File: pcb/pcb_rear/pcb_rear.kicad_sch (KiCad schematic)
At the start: 23 parts, among them J1 MicroLab Input, J2 Pump, J3 DFRobot O2, J4 DFRobot NH3, Q1 T2N7002AK, Q2 T2N7002AK, Q3 T2N7002AK, Q4 T2N7002AK, U1 USEQGSE CO2, U2 USEQGSE CH4, U3 XC9265A331MR-G, U4 XC9265A331MR-G

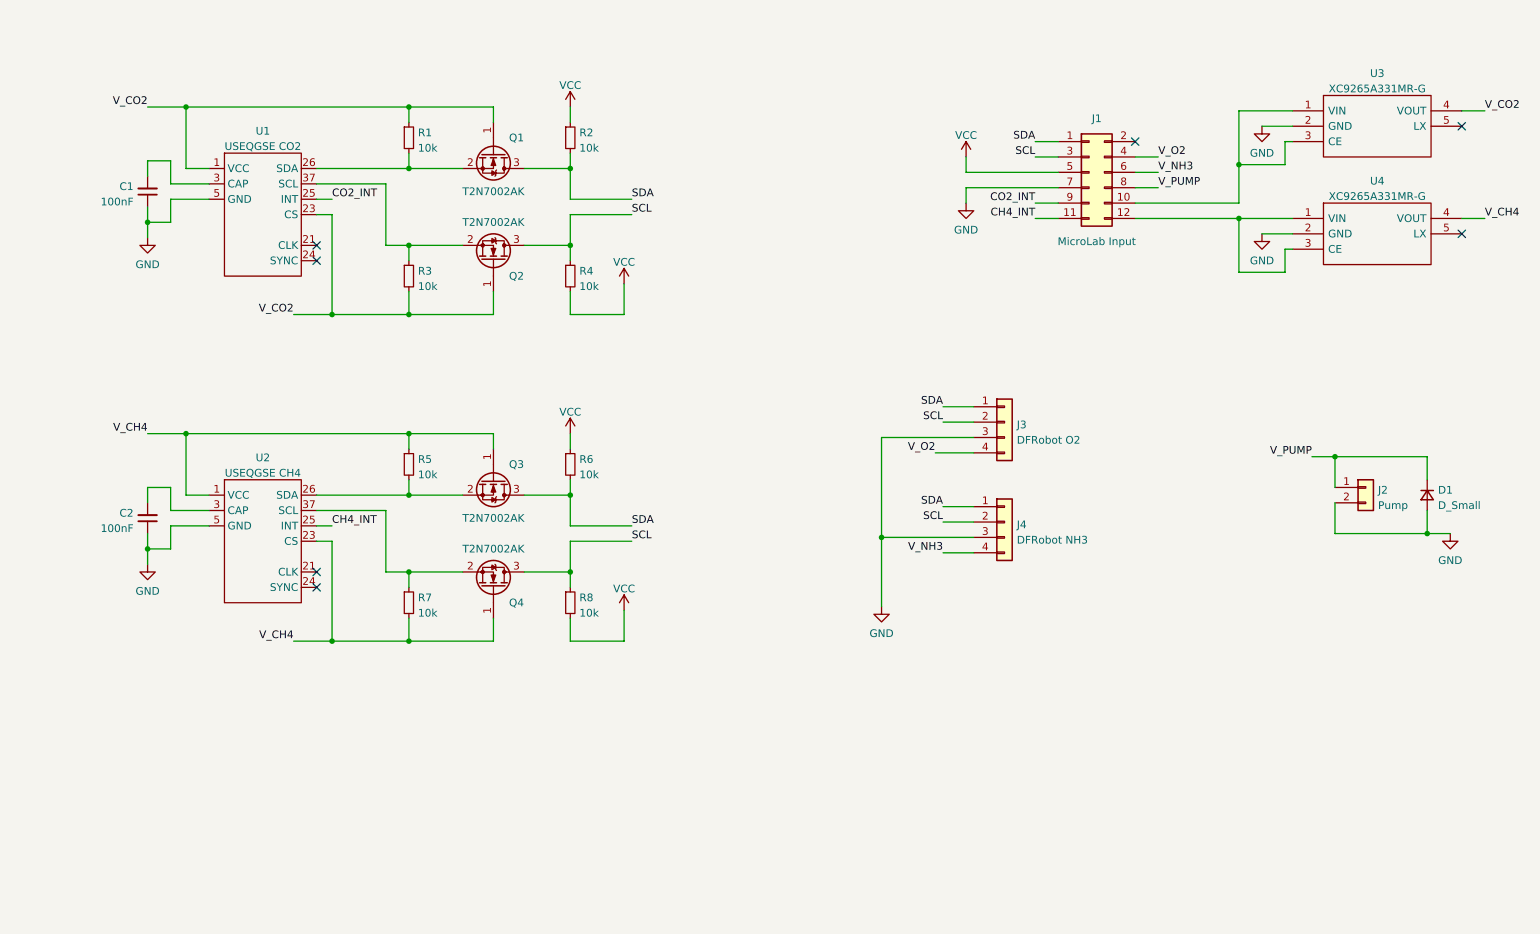
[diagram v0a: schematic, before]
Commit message: renamed pcb
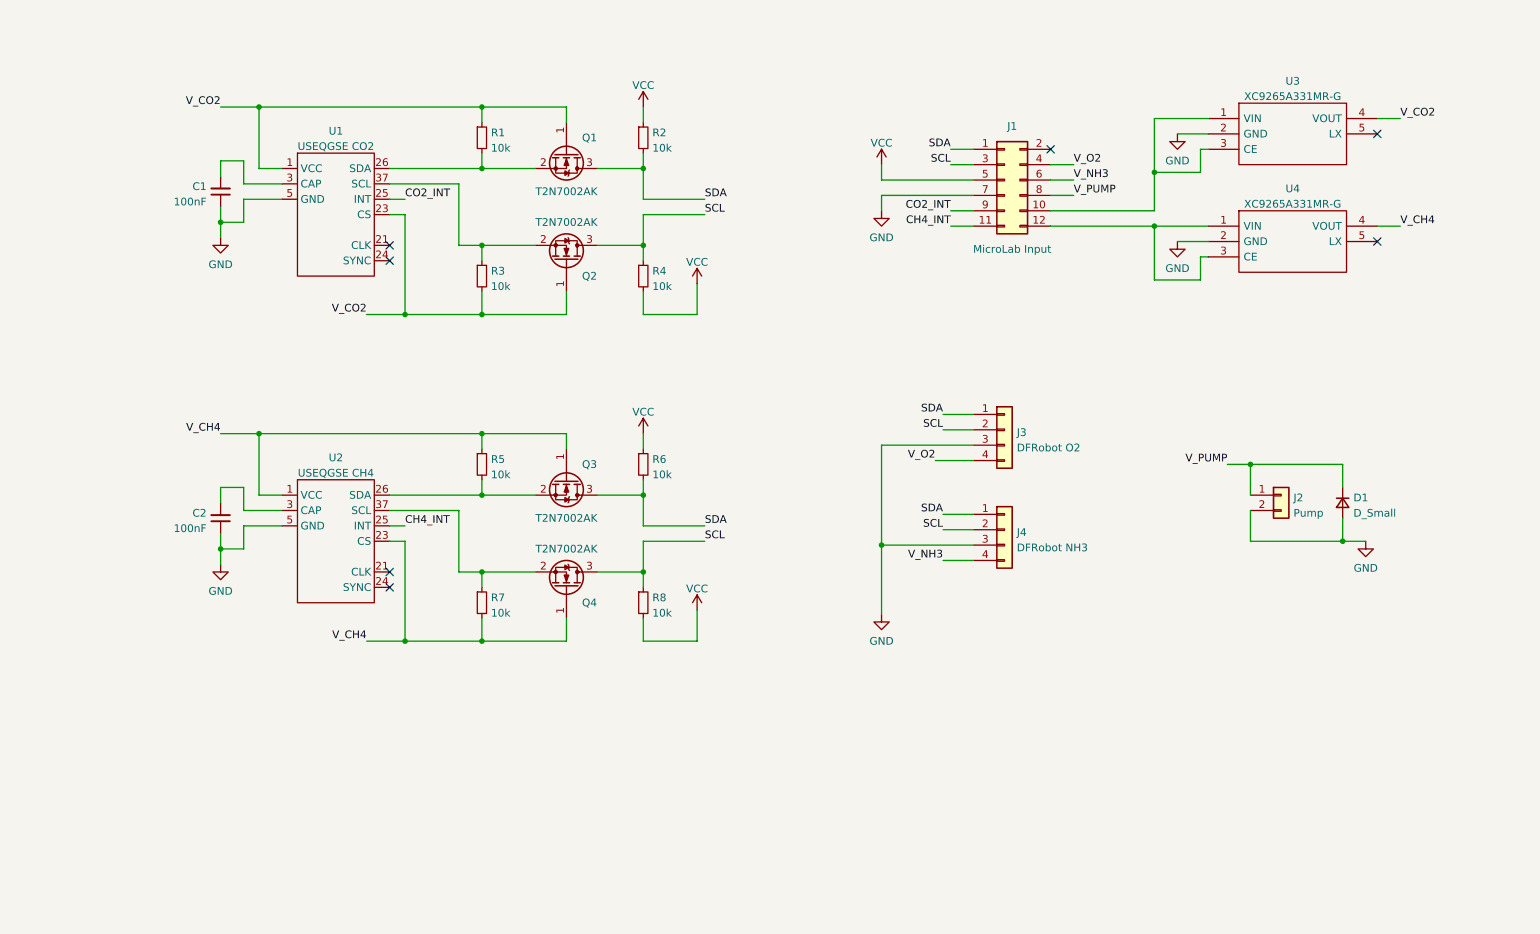
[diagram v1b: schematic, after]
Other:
- moved on the sheet: C1, C2, D1, J1, J2, J3, J4, Q1, Q2, Q3, Q4, R1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

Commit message: front pcb 1st rev
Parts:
- removed U3, U4: XC9265A331MR-G, SamacSys:SOT95P280X130-5N, symbol SamacSys:XC9265A331MR-G
- added D2: D_Small, Diode_SMD:D_0603_1608Metric, symbol Device:D_Small
- added J5: Fan, Connector_PinSocket_2.54mm:PinSocket_1x02_P2.54mm_Vertical, symbol Connector_Generic:Conn_01x02
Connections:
- net GND: now also D2.2 (A), J5.2 (Pin_2)
- net V_CH4: now also J1.12 (Pin_12)
- net V_CO2: now also J1.10 (Pin_10)
- net V_NH3: now also J1.8 (Pin_8); no longer J1.6 (Pin_6)
- net V_O2: now also J1.6 (Pin_6); no longer J1.4 (Pin_4)
- net V_PUMP: now also J1.4 (Pin_4); no longer J1.8 (Pin_8)
- net V_FAN: now reaches J1.2 (Pin_2)
- net V_FAN: now also D2.1 (K), J5.1 (Pin_1)
- no-connect marks 7 -> 4
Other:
- moved on the sheet: D1, J1, J2, J3, J4

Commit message: fin
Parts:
- removed C2: 100nF, Capacitor_SMD:C_0603_1608Metric, symbol Device:C_Small
- removed J1: MicroLab Input, Connector_PinSocket_2.54mm:PinSocket_2x06_P2.54mm_Vertical, symbol Connector_Generic:Conn_02x06_Odd_Even
- removed J2: Pump, Connector_PinSocket_2.54mm:PinSocket_1x02_P2.54mm_Vertical, symbol Connector_Generic:Conn_01x02
- removed J3: DFRobot O2, Connector_PinSocket_2.54mm:PinSocket_1x04_P2.54mm_Vertical, symbol Connector_Generic:Conn_01x04
- removed J4: DFRobot NH3, Connector_PinSocket_2.54mm:PinSocket_1x04_P2.54mm_Vertical, symbol Connector_Generic:Conn_01x04
- removed J5: Fan, Connector_PinSocket_2.54mm:PinSocket_1x02_P2.54mm_Vertical, symbol Connector_Generic:Conn_01x02
- removed Q1, Q2, Q3, Q4: T2N7002AK, Package_TO_SOT_SMD:SOT-23, symbol Transistor_FET:BSS138
- added C1, C3, C5, C6, C7: 0.1uF, Capacitor_SMD:C_0402_1005Metric, symbol Device:C_Small
- added C4, C8: 10uF, Capacitor_SMD:C_0402_1005Metric, symbol Device:C_Small
- added D3: PWR, LED_SMD:LED_0402_1005Metric, symbol Device:LED_Small
- added H1, H2, H3, H4: M2, MountingHole:MountingHole_2.2mm_M2_DIN965_Pad, symbol Mechanical:MountingHole_Pad
- added J1: XIAO_L, Connector_PinSocket_2.54mm:PinSocket_1x07_P2.54mm_Vertical, symbol Connector_Generic:Conn_01x07
- added J2: XIAO_R, Connector_PinSocket_2.54mm:PinSocket_1x07_P2.54mm_Vertical, symbol Connector_Generic:Conn_01x07
- added J3: MicroLab, Connector_JST:JST_SH_BM04B-SRSS-TB_1x04-1MP_P1.00mm_Vertical, symbol Connector_Generic_MountingPin:Conn_01x04_MountingPin
- added J4: O2 Sensor, Connector_JST:JST_SH_BM04B-SRSS-TB_1x04-1MP_P1.00mm_Vertical, symbol Connector_Generic_MountingPin:Conn_01x04_MountingPin
- added J5: Fan, Connector_JST:JST_SH_BM02B-SRSS-TB_1x02-1MP_P1.00mm_Vertical, symbol Connector_Generic_MountingPin:Conn_01x02_MountingPin
- added J8: MEM2051-00-195-00-A, SamacSys:MEM20510019500A, symbol Mouser Parts:MEM2051-00-195-00-A
- added Q1: NX7002BKR, Package_TO_SOT_SMD:SOT-23, symbol Mouser Parts:NX7002BKR
- added R9: 500, Resistor_SMD:R_0402_1005Metric, symbol Device:R_Small
- C2: renamed from C1; value 100nF -> 0.1uF; footprint Capacitor_SMD:C_0603_1608Metric -> Capacitor_SMD:C_0402_1005Metric
- D1, D2: footprint Diode_SMD:D_0603_1608Metric -> Diode_SMD:D_SOD-323
- R1, R2, R3, R4, R5: value 10k -> 50k; footprint Resistor_SMD:R_0603_1608Metric -> Resistor_SMD:R_0402_1005Metric
- R6, R7, R8: footprint Resistor_SMD:R_0603_1608Metric -> Resistor_SMD:R_0402_1005Metric
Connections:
- net V_CH4 is gone; now on net +3.3V: R5.1, R7.2, U2.1 (VCC), U2.23 (CS)
- net GND: now also R8.1, C1.1, C3.1, C4.1, C5.1, C6.1, C7.1, C8.1, D3.1 (K), H1.1, H2.1, H3.1, H4.1, J1.2 (Pin_2), J3.4 (Pin_4), J3.MP (MountPin), J4.2 (Pin_2), J4.MP (MountPin), J8.MP1, J8.MP2, J8.MP3, J8.MP4, J8.MP5, J8.P6 (VSS), Q1.2; no longer D1.2 (A), D2.2 (A)
- net SCL: now also R7.1, U1.27 (SCL), U2.27 (SCL), J2.6 (Pin_6), J4.4 (Pin_4); no longer R4.1, R8.1
- net SDA: now also R6.1, U1.26 (SDA), U2.26 (SDA), J2.5 (Pin_5), J4.3 (Pin_3); no longer R2.2, R6.2
- net at R5.2: now also J8.P8 (DAT1); no longer U2.26 (SDA)
- net +3.3V: now reaches R3.1
- net +3.3V: now also R1.1, R2.1, R4.1, R6.2, U1.1 (VCC), U1.23 (CS), C1.2, C3.2, C4.2, C6.2, C7.2, C8.2, J1.3 (Pin_3), J4.1 (Pin_1), J8.P4 (VDD); no longer U1.37 (SCL)
- net at U2.3 (CAP): now also C5.2
- net at R1.2: now also J8.P1 (DAT2); no longer U1.26 (SDA)
- net CH4_INT: no longer names the net of U2.25 (INT)
- net CO2_INT: no longer names the net of U1.25 (INT)
- removed net VCC: R2.1, R4.2, R6.1, R8.2
- removed net V_CO2: R1.1, R3.2, U1.1 (VCC), U1.23 (CS)
- net V_FAN renamed +5V
- net +5V: now also D1.2 (A), J1.1 (Pin_1), J5.1 (Pin_1), R9.2
- net V_PUMP: no longer names the net of D1.1 (K)
- net V_PUMP: now also J3.1 (Pin_1)
- new net: D2.2 (A), J5.2 (Pin_2), J5.MP (MountPin), Q1.3
- new net: D3.2 (A), R9.1
- new net D0: J2.1 (Pin_1), J8.P2 (CD/DAT3), R2.2
- new net D1: J2.2 (Pin_2), Q1.1, R8.2
- new net MISO: J1.5 (Pin_5), J8.P7 (DAT0), R4.2
- new net MOSI: J1.4 (Pin_4), J8.P3 (CMD), R3.2
- new net P2: J2.3 (Pin_3)
- new net P3: J2.4 (Pin_4)
- new net RX: J2.7 (Pin_7), J3.2 (Pin_2)
- new net SCK: J1.6 (Pin_6), J8.P5 (CLK)
- new net TX: J1.7 (Pin_7), J3.3 (Pin_3)
- no-connect marks 4 -> 6
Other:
- note added: "NOTE: SEEEDUINO XIAO IS 3.3V LOGIC"
- note added: "Protects MicroLab from Seeeduino Xiao USB power"
- moved on the sheet: C2, D2, U1

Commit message: goodnight
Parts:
- R1, R2, R3, R4: value 50k -> 10k
- R9: value 500 -> 2k
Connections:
- net +5V: now also D1.1 (K); no longer D1.2 (A)
- net at J3.1 (Pin_1): now also D1.2 (A); no longer D1.1 (K)
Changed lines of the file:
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@@
       (effects (font (size 1.27 1.27)) (justify left))
     )
-    (property "Value" "50k" (id 1) (at 212.3186 57.5822 0)
+    (property "Value" "10k" (id 1) (at 212.3186 57.5822 0)
       (effects (font (size 1.27 1.27)) (justify left))
     )
@@
       (effects (font (size 1.27 1.27)) (justify left))
     )
-    (property "Value" "50k" (id 1) (at 204.6986 57.5822 0)
+    (property "Value" "10k" (id 1) (at 204.6986 57.5822 0)
       (effects (font (size 1.27 1.27)) (justify left))
     )
@@
       (effects (font (size 1.27 1.27)) (justify left))
     )
-    (property "Value" "50k" (id 1) (at 189.4586 57.5822 0)
+    (property "Value" "10k" (id 1) (at 189.4586 57.5822 0)
       (effects (font (size 1.27 1.27)) (justify left))
     )
@@
     (pin "MP")
   )
-  (symbol (lib_id "Device:D_Small") (at 208.28 125.73 90) (unit 1)
-    (in_bom yes) (on_board yes)
-    (property "Reference" "D1" (id 0) (at 206.756 124.714 90)
-      (effects (font (size 1.27 1.27)) (justify left))
-    )
-    (property "Value" "D_Small" (id 1) (at 206.502 127.508 90)
+  (symbol (lib_id "Device:D_Small") (at 208.28 125.73 90) (mirror x) (unit 1)
+    (in_bom yes) (on_board yes)
+    (property "Reference" "D1" (id 0) (at 206.756 127.254 90)
+      (effects (font (size 1.27 1.27)) (justify left))
+    )
+    (property "Value" "D_Small" (id 1) (at 206.502 124.714 90)
       (effects (font (size 1.27 1.27)) (justify left))
     )
@@
       (effects (font (size 1.27 1.27)) (justify right))
     )
-    (property "Value" "500" (id 1) (at 153.1366 135.8142 0)
+    (property "Value" "2k" (id 1) (at 153.1366 135.8142 0)
       (effects (font (size 1.27 1.27)) (justify right))
     )
@@
       (effects (font (size 1.27 1.27)) (justify left))
     )
-    (property "Value" "50k" (id 1) (at 197.0786 57.5822 0)
+    (property "Value" "10k" (id 1) (at 197.0786 57.5822 0)
       (effects (font (size 1.27 1.27)) (justify left))
     )
@@
     )
     (path "/4ef94825-aecc-4a50-b058-09fd3aae0868"
-      (reference "R1") (unit 1) (value "50k") (footprint "Resistor_SMD:R_0402_1005Metric")
+      (reference "R1") (unit 1) (value "10k") (footprint "Resistor_SMD:R_0402_1005Metric")
     )
     (path "/7e78a2b9-7270-443c-b68a-25c56931dde8"
-      (reference "R2") (unit 1) (value "50k") (footprint "Resistor_SMD:R_0402_1005Metric")
+      (reference "R2") (unit 1) (value "10k") (footprint "Resistor_SMD:R_0402_1005Metric")
     )
     (path "/f6999765-fdb3-447c-9a43-c47833c25696"
-      (reference "R3") (unit 1) (value "50k") (footprint "Resistor_SMD:R_0402_1005Metric")
+      (reference "R3") (unit 1) (value "10k") (footprint "Resistor_SMD:R_0402_1005Metric")
     )
     (path "/9d303d19-fad4-45e0-bf5d-19c5634ca9ff"
-      (reference "R4") (unit 1) (value "50k") (footprint "Resistor_SMD:R_0402_1005Metric")
+      (reference "R4") (unit 1) (value "10k") (footprint "Resistor_SMD:R_0402_1005Metric")
     )
     (path "/88783343-3330-48a7-b3ee-8d85118d5748"
@@
     )
     (path "/f36363d8-d592-4975-b4e3-ab59ffe2f770"
-      (reference "R9") (unit 1) (value "500") (footprint "Resistor_SMD:R_0402_1005Metric")
+      (reference "R9") (unit 1) (value "2k") (footprint "Resistor_SMD:R_0402_1005Metric")
     )
     (path "/eee5664e-be1d-485d-90e4-ea8c5294c7f4"
